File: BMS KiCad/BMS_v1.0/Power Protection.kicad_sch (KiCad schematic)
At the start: 8 parts, among them J1 Conn_01x02, J2 Conn_01x02, Q1 PMOS, Q2 PMOS, U2 INA193

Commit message: power protection done pretty much
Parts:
- added C10: 0.047u, symbol Device:C
- added D1: Q_SCR_KAG, symbol Device:Q_SCR_KAG
- added D2: 20V, symbol Device:D_Zener
- added D3: D_Zener, symbol Device:D_Zener
- added D4: LED, symbol Device:LED
- added Q3, Q4: NMOS, symbol Simulation_SPICE:NMOS
- added R3: 1k, symbol Device:R
- added R4, R5: 10k, symbol Device:R
- added TP1: BAT+, symbol Connector:TestPoint
- added TP2: BAT+ PROT, symbol Connector:TestPoint
- F2: value Fuse -> 500mA
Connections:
- net GND: now also C10.2, D1.1 (K), R3.2, R4.2, R5.2
- net at F2.1: now also Q1.1 (D), D1.2 (A)
- net at F1.1, R2.1: now also TP1.1
- net at R2.4: now also Q3.1 (D); no longer J2.2 (Pin_2)
- net at Q1.2 (G): now also Q2.2 (G), D2.2 (A), R3.1
- net at Q1.3 (S): now also Q2.3 (S), D2.1 (K)
- net BAT Protected: now reaches Q2.1 (D)
- net BAT Protected: now also D3.1 (K), D4.2 (A), TP2.1
- new net: C10.1, D1.3 (G), D3.2 (A), R4.1
- new net: Q3.3 (S), Q4.3 (S)
- new net: D4.1 (K), R5.1
- new net: J2.2 (Pin_2), Q4.1 (D)
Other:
- note added: "crowbar power protection circuit for LV"
- note added: "need gate driver and control from MCU for common source blocking nmos"
- moved on the sheet: F2, J2, Q1, Q2, R2, U2

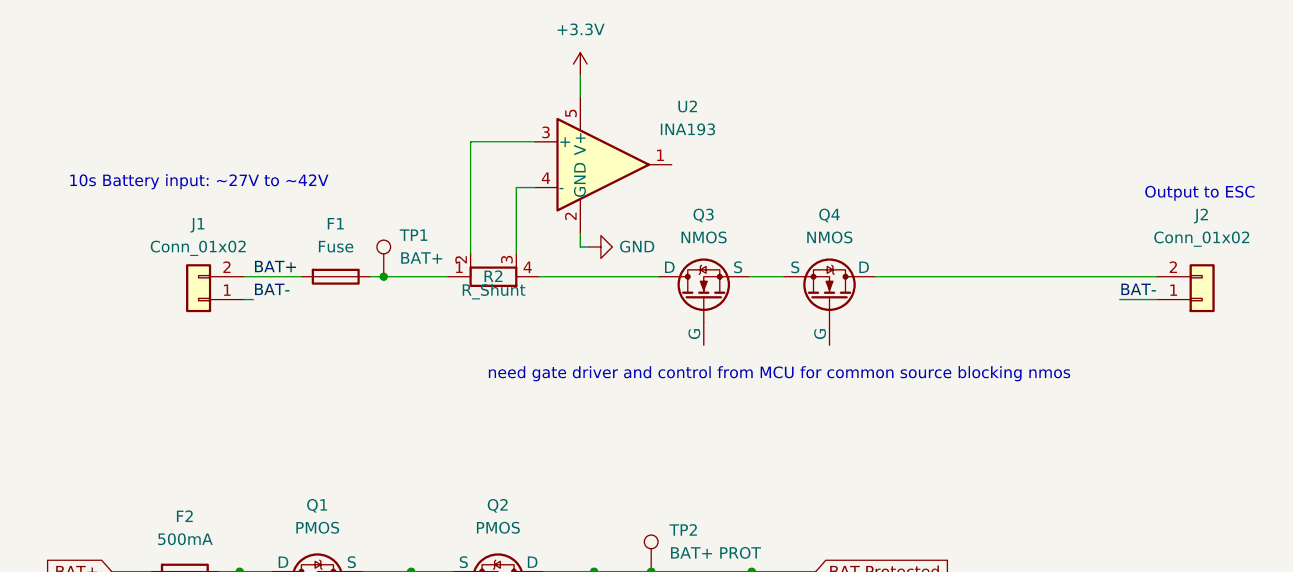
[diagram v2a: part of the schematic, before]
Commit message: added thermistor and shunts to battery monitoring ic
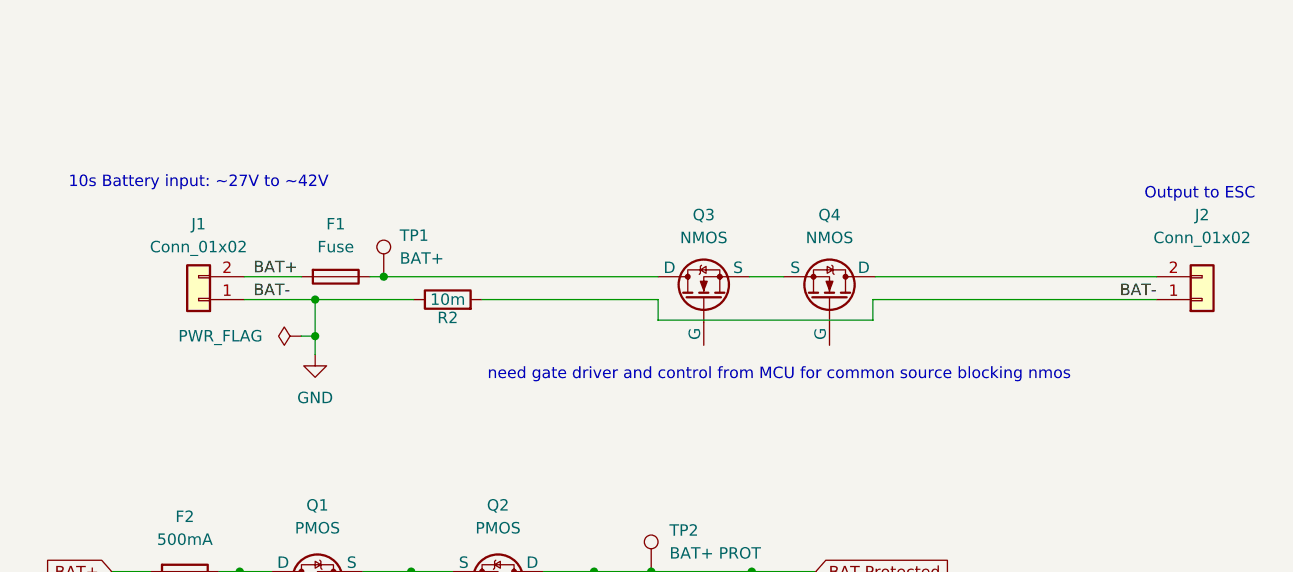
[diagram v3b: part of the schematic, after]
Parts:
- removed R2: R_Shunt, symbol Device:R_Shunt
- removed U2: INA193, Package_TO_SOT_SMD:SOT-23-5, symbol Amplifier_Current:INA193
- added R2: 10m, symbol Device:R
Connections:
- net BAT- is gone; now on net GND: J1.1 (Pin_1), J2.1 (Pin_1)
- net GND: now also R2.1, R2.2
- net at Q3.1 (D): now also F1.1, TP1.1

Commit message: TI IC done except for I2C and precharge circuit
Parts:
- added C26: 0.1u, symbol Device:C_Small
- added C27: 100p, symbol Device:C_Small
- added D6, D7: 16V, symbol Device:D_Zener
- added R18, R19: 100, symbol Device:R
- added R20, R21, R24, R25: 5.1k, symbol Device:R
- added R22: 10k, symbol Device:R
- added R23, R26: 10M, symbol Device:R
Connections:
- net GND: now also R18.1, R19.1
- net at F1.1, TP1.1: now also Q3.3 (S), D6.2 (A), R23.1; no longer Q3.1 (D)
- net at Q3.2 (G): now also D6.1 (K), R23.2, R24.1
- net at Q4.3 (S): now also J2.2 (Pin_2), D7.2 (A), R20.1, R22.1, R26.1; no longer Q3.3 (S)
- net at Q4.1 (D): now also Q3.1 (D); no longer J2.2 (Pin_2)
- net at Q4.2 (G): now also D7.1 (K), R25.1, R26.2
- new net: R20.2, R21.1
- new net CHG: R24.2
- new net DSG: R25.2
- new net LD: R22.2
- new net PACK: R21.2
- new net SRN: C26.2, C27.2, R19.2
- new net SRP: C26.1, C27.1, R18.2
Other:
- note added: "Common Drain high side NMOS Controlled by TI IC"
- note added: "RC filter for shunt"
- note removed: "need gate driver and control from MCU for common source blocking nmos"
- moved on the sheet: F1, J1, J2, Q3, Q4, R2, TP1

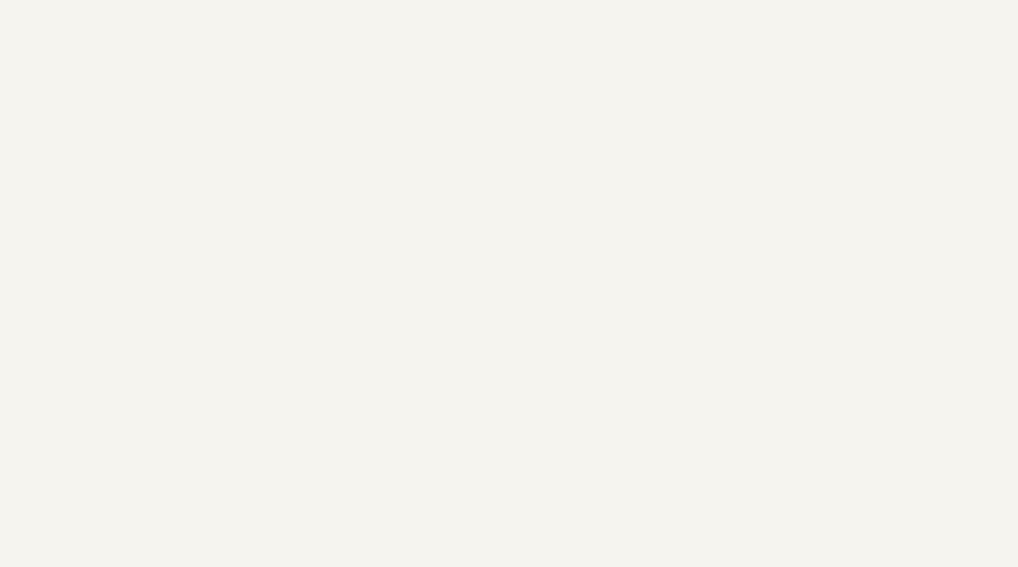
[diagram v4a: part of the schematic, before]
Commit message: footprints for almost everything
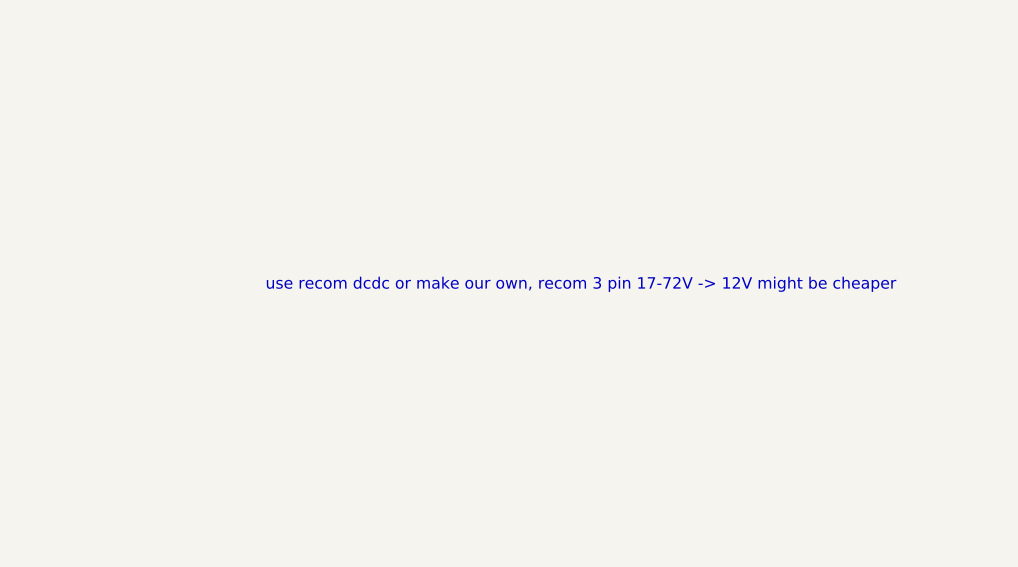
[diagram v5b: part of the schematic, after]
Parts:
- C10, C26, C27: footprint (none) -> Capacitor_SMD:C_0603_1608Metric_Pad1.08x0.95mm_HandSolder
- D2, D3, D4, D6, D7: footprint (none) -> Diode_SMD:D_0603_1608Metric_Pad1.05x0.95mm_HandSolder
- F2, R2, R3, R4, R5: footprint (none) -> Fuse:Fuse_0603_1608Metric_Pad1.05x0.95mm_HandSolder
- R18, R19, R20, R21, R22, R23, R24, R25, R26: footprint (none) -> Resistor_SMD:R_0603_1608Metric_Pad0.98x0.95mm_HandSolder
- TP1, TP2: footprint (none) -> TestPoint:TestPoint_Pad_1.0x1.0mm
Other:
- note added: "use recom dcdc or make our own, recom 3 pin 17-72V -> 12V might be cheaper"
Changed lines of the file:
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@@
 		)
 	)
+	(text "use recom dcdc or make our own, recom 3 pin 17-72V -> 12V might be cheaper\n"
+		(exclude_from_sim no)
+		(at 208.788 83.312 0)
+		(effects
+			(font
+				(size 1.27 1.27)
+			)
+		)
+	)
 	(text "crowbar power protection circuit for LV"
 		(exclude_from_sim no)
@@
 			)
 		)
-		(property "Footprint" ""
+		(property "Footprint" "Resistor_SMD:R_0603_1608Metric_Pad0.98x0.95mm_HandSolder"
 			(at 133.858 50.8 90)
 			(effects
@@
 			)
 		)
-		(property "Footprint" ""
+		(property "Footprint" "Resistor_SMD:R_0603_1608Metric_Pad0.98x0.95mm_HandSolder"
 			(at 69.342 42.164 90)
 			(effects
@@
 			)
 		)
-		(property "Footprint" ""
+		(property "Footprint" "Resistor_SMD:R_0603_1608Metric_Pad0.98x0.95mm_HandSolder"
 			(at 144.526 40.386 90)
 			(effects
@@
 			)
 		)
-		(property "Footprint" ""
+		(property "Footprint" "Resistor_SMD:R_0603_1608Metric_Pad0.98x0.95mm_HandSolder"
 			(at 162.56 21.336 90)
 			(effects
@@
 			)
 		)
-		(property "Footprint" ""
+		(property "Footprint" "Capacitor_SMD:C_0603_1608Metric_Pad1.08x0.95mm_HandSolder"
 			(at 98.5012 110.49 0)
 			(effects
@@
 			)
 		)
-		(property "Footprint" ""
+		(property "Footprint" "Diode_SMD:D_0603_1608Metric_Pad1.05x0.95mm_HandSolder"
 			(at 101.346 40.386 0)
 			(effects
@@
 			)
 		)
-		(property "Footprint" ""
+		(property "Footprint" "TestPoint:TestPoint_Pad_1.0x1.0mm"
 			(at 108.966 80.01 0)
 			(effects
@@
 			)
 		)
-		(property "Footprint" ""
+		(property "Footprint" "Fuse:Fuse_0603_1608Metric_Pad1.05x0.95mm_HandSolder"
 			(at 84.074 106.68 90)
 			(effects
@@
 			)
 		)
-		(property "Footprint" ""
+		(property "Footprint" "Capacitor_SMD:C_0603_1608Metric_Pad1.08x0.95mm_HandSolder"
 			(at 76.962 57.404 0)
 			(effects
@@
 			)
 		)
-		(property "Footprint" ""
+		(property "Footprint" "Capacitor_SMD:C_0603_1608Metric_Pad1.08x0.95mm_HandSolder"
 			(at 76.962 52.578 0)
 			(effects
@@
 			)
 		)
-		(property "Footprint" ""
+		(property "Footprint" "Resistor_SMD:R_0603_1608Metric_Pad0.98x0.95mm_HandSolder"
 			(at 80.518 41.91 90)
 			(effects
@@
 			)
 		)
-		(property "Footprint" ""
+		(property "Footprint" "Fuse:Fuse_0603_1608Metric_Pad1.05x0.95mm_HandSolder"
 			(at 76.962 37.084 90)
 			(effects
@@
 			)
 		)
-		(property "Footprint" ""
+		(property "Footprint" "Diode_SMD:D_0603_1608Metric_Pad1.05x0.95mm_HandSolder"
 			(at 154.178 40.132 0)
 			(effects
@@
 			)
 		)
-		(property "Footprint" ""
+		(property "Footprint" "TestPoint:TestPoint_Pad_1.0x1.0mm"
 			(at 74.93 32.766 0)
 			(effects
@@
 			)
 		)
-		(property "Footprint" ""
+		(property "Footprint" "Diode_SMD:D_0603_1608Metric_Pad1.05x0.95mm_HandSolder"
 			(at 77.216 85.09 0)
 			(effects
@@
 			)
 		)
-		(property "Footprint" ""
+		(property "Footprint" "Fuse:Fuse_0603_1608Metric_Pad1.05x0.95mm_HandSolder"
 			(at 52.07 78.232 90)
 			(effects
@@
 			)
 		)
-		(property "Footprint" ""
+		(property "Footprint" "Resistor_SMD:R_0603_1608Metric_Pad0.98x0.95mm_HandSolder"
 			(at 107.95 40.386 90)
 			(effects
@@
 			)
 		)
-		(property "Footprint" ""
+		(property "Footprint" "Fuse:Fuse_0603_1608Metric_Pad1.05x0.95mm_HandSolder"
 			(at 113.284 101.346 90)
 			(effects
@@
 			)
 		)
-		(property "Footprint" ""
+		(property "Footprint" "Fuse:Fuse_0603_1608Metric_Pad1.05x0.95mm_HandSolder"
 			(at 75.438 96.266 90)
 			(effects
@@
 			)
 		)
-		(property "Footprint" ""
+		(property "Footprint" "Resistor_SMD:R_0603_1608Metric_Pad0.98x0.95mm_HandSolder"
 			(at 171.704 21.336 90)
 			(effects
@@
 			)
 		)
-		(property "Footprint" ""
+		(property "Footprint" "Diode_SMD:D_0603_1608Metric_Pad1.05x0.95mm_HandSolder"
 			(at 115.062 91.948 0)
 			(effects
@@
 			)
 		)
-		(property "Footprint" ""
+		(property "Footprint" "Resistor_SMD:R_0603_1608Metric_Pad0.98x0.95mm_HandSolder"
 			(at 165.862 27.686 90)
 			(effects
@@
 			)
 		)
-		(property "Footprint" ""
+		(property "Footprint" "Resistor_SMD:R_0603_1608Metric_Pad0.98x0.95mm_HandSolder"
 			(at 119.888 50.8 90)
 			(effects
@@
 			)
 		)
-		(property "Footprint" ""
+		(property "Footprint" "Diode_SMD:D_0603_1608Metric_Pad1.05x0.95mm_HandSolder"
 			(at 97.536 89.916 0)
 			(effects
